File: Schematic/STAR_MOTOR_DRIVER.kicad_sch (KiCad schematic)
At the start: 50 parts, among them J1 6120XX21621_61200621621, J10 Optical Encoder 1, J11 Optical Encoder 2, J2 6120XX21621_61200621621, J3 1017491, J4 6120XX21621_61200821621, J5 6120XX21621_61200821621, J6 6120XX21621_61200821621, J7 1017491, J8 1017491, J9 1017491, U1 DRV8243SQDGQRQ1 (S-Variant), U2 DRV8243SQDGQRQ1 (S-Variant), U3 DRV8243SQDGQRQ1 (S-Variant), U4 DRV8243SQDGQRQ1 (S-Variant), U5 74LVC125APW_118

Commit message: Motor Driver PCB Design 1.0.0
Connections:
- net GND: now also J3.3 (2.1), J7.3 (2.1); no longer J3.2 (1.2), J7.2 (1.2)
- net MOTOR3_TERMINAL1: now also J9.1 (1.1); no longer J9.4 (2.2)
- net MOTOR3_TERMINAL2: now also J9.4 (2.2); no longer J9.1 (1.1)
- net MOTOR4_TERMINAL1: now also J8.1 (1.1); no longer J8.4 (2.2)
- net MOTOR4_TERMINAL2: now also J8.4 (2.2); no longer J8.1 (1.1)
- net P5V0_BUCK: now also J3.2 (1.2); no longer J3.3 (2.1)
- net P6V0_BUCK: now also J7.2 (1.2); no longer J7.3 (2.1)
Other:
- company: (none) -> Locked Inc.
- title: (none) -> Motor Driver

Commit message: Version 1.1.1
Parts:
- removed C13, C15, C17: 1u, Capacitor_SMD:C_0603_1608Metric_Pad1.08x0.95mm_HandSolder, symbol Device:C
- removed C14, C16, C18: 100n, Capacitor_SMD:C_0603_1608Metric_Pad1.08x0.95mm_HandSolder, symbol Device:C
- removed J1: 6120XX21621_61200621621, 61200621621:61200621621, symbol 61200621621:6120XX21621_61200621621
- removed J10: Optical Encoder 1, Connector_PinHeader_2.54mm:PinHeader_1x06_P2.54mm_Vertical, symbol Connector_Generic:Conn_01x06
- removed J11: Optical Encoder 2, Connector_PinHeader_2.54mm:PinHeader_1x06_P2.54mm_Vertical, symbol Connector_Generic:Conn_01x06
- removed J3, J8, J9: 1017491, 1017491, symbol 1017491:1017491
- removed U5: 74LVC125APW_118, 74LVC125APW,118:SOP65P640X110-14N, symbol 74LVC125APW-118:74LVC125APW_118
- added J1: 6120XX21621_61200821621, 6120XX21621_61200821621:61200821621, symbol 61200821621:6120XX21621_61200821621
- added J10, J3: B6B-XH-A, B6B_XH_A-2:JST_B6B-XH-A, symbol B6B-XH-A:B6B-XH-A
- added J11, J12: B6B-XH-A, B6B-XH-A:JST_B6B-XH-A, symbol B6B-XH-A:B6B-XH-A
- R10, R11, R12, R9: value 1k69 -> 3k16
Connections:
- net GND: now also J2.2, J2.4, J1.8, J10.2, J11.2, J12.2, J3.2; no longer J2.5
- net P3V3_BUCK: now also J2.1, J2.3, J2.5, J10.5, J11.5, J12.5, J3.5
- net ENCODER1_OUTPUT1 renamed MCU_ENCODER1_INPUT_B
- net MCU_ENCODER1_INPUT_B: now also J3.4
- net ENCODER1_OUTPUT2 renamed MCU_ENCODER2_INPUT_B
- net MCU_ENCODER2_INPUT_B: now also J10.4
- net ENCODER2_OUTPUT1 renamed MCU_ENCODER3_INPUT_B
- net MCU_ENCODER3_INPUT_B: now also J11.4
- net ENCODER2_OUTPUT2 renamed MCU_ENCODER4_INPUT_B
- net MCU_ENCODER4_INPUT_B: now also J12.4
- net MOTOR1_EN_IN1 renamed MCU_MOTOR1_EN_IN1
- net MOTOR1_IPROPI renamed MCU_MOTOR1_IPROPI
- net MOTOR1_PH_IN2 renamed MCU_MOTOR1_PH_IN2
- net MOTOR1_TERMINAL1 renamed MOTOR1_VCC
- net MOTOR1_VCC: now also J3.6; no longer J6.1
- net MOTOR1_TERMINAL2 renamed MOTOR1_VEE
- net MOTOR1_VEE: now also J3.1; no longer J6.3
- net MOTOR1_nCS renamed MCU_MOTOR1_nCS
- net MCU_MOTOR1_nCS: now also J1.1; no longer J2.1
- net MOTOR1_nFAULT renamed MCU_MOTOR1_nFAULT
- net MOTOR2_EN_IN1 renamed MCU_MOTOR2_EN_IN1
- net MOTOR2_IPROPI renamed MCU_MOTOR2_IPROPI
- net MOTOR2_PH_IN2 renamed MCU_MOTOR2_PH_IN2
- net MOTOR2_TERMINAL1 renamed MOTOR2_VCC
- net MOTOR2_VCC: now also J10.6; no longer J6.5
- net MOTOR2_TERMINAL2 renamed MOTOR2_VEE
- net MOTOR2_VEE: now also J10.1; no longer J6.7
- net MOTOR2_nCS renamed MCU_MOTOR2_nCS
- net MCU_MOTOR2_nCS: now also J1.3; no longer J2.2
- net MOTOR2_nFAULT renamed MCU_MOTOR2_nFAULT
- net MOTOR3_EN_IN1 renamed MCU_MOTOR3_EN_IN1
- net MOTOR3_IPROPI renamed MCU_MOTOR3_IPROPI
- net MOTOR3_PH_IN2 renamed MCU_MOTOR3_PH_IN2
- net MOTOR3_TERMINAL1 renamed MOTOR3_VCC
- net MOTOR3_VCC: now also J11.6
- net MOTOR3_TERMINAL2 renamed MOTOR3_VEE
- net MOTOR3_VEE: now also J11.1
- net MOTOR3_nCS renamed MCU_MOTOR3_nCS
- net MCU_MOTOR3_nCS: now also J1.5; no longer J2.4
- net MOTOR3_nFAULT renamed MCU_MOTOR3_nFAULT
- net MOTOR4_EN_IN1 renamed MCU_MOTOR4_EN_IN1
- net MOTOR4_IPROPI renamed MCU_MOTOR4_IPROPI
- net MOTOR4_PH_IN2 renamed MCU_MOTOR4_PH_IN2
- net MOTOR4_TERMINAL1 renamed MOTOR4_VCC
- net MOTOR4_VCC: now also J12.6
- net MOTOR4_TERMINAL2 renamed MOTOR4_VEE
- net MOTOR4_VEE: now also J12.1
- net MOTOR4_nCS renamed MCU_MOTOR4_nCS
- net MCU_MOTOR4_nCS: now also J1.7; no longer J2.3
- net MOTOR4_nFAULT renamed MCU_MOTOR4_nFAULT
- net SPI_CIPO renamed MCU_SPI_CIPO
- net MCU_SPI_CIPO: now also J1.6
- net SPI_COPI renamed MCU_SPI_COPI
- net MCU_SPI_COPI: now also J1.2
- net SPI_SCLK renamed MCU_SPI_SCLK
- net MCU_SPI_SCLK: now also J1.4
- new net MCU_ENCODER1_INPUT_A: J3.3, J6.1
- new net MCU_ENCODER2_INPUT_A: J10.3, J6.3
- new net MCU_ENCODER3_INPUT_A: J11.3, J6.5
- new net MCU_ENCODER4_INPUT_A: J12.3, J6.7
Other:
- note added: "input line is 20A, 4 motots, 3A eash, ADC overhead, 3.2A I_MCU_MOTOR = I_IPROPI x A_IPROPI 3.2A = I_IPROPI x 3075. I_PROPI=0.00104065 3.3V = 0.001041A x R, R = 3171.1 -> 3k16"
- note removed: "Input has to be 5V, output has to be 3V3"
- note removed: "input line is 20A, 4 motors, 5A each, ADC overhead, 6A I_motor = I_IPROPI x A_IPROPI 6A = I_IPROPI x 3075, I_IPROPI=0.00195121951 3.3V = 0.00195A x R, R = 1692.3 -> 1k69 WITH CODE: Shut off the motors at 4A"
- moved on the sheet: J2, J5, J6, J7

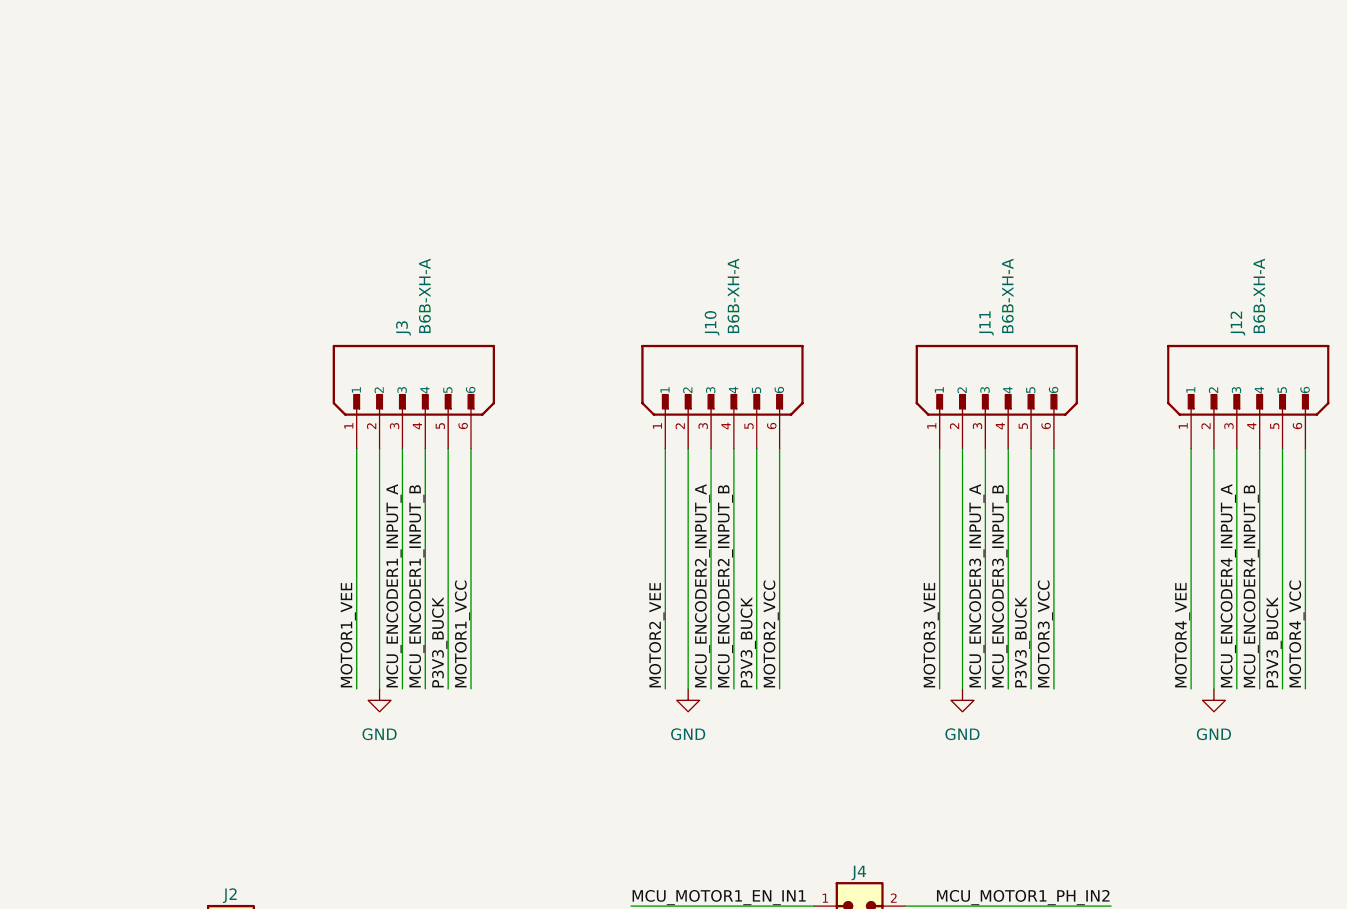
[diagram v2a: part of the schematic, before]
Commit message: V1.1.1 (Actual)
only changes are colors on schematic
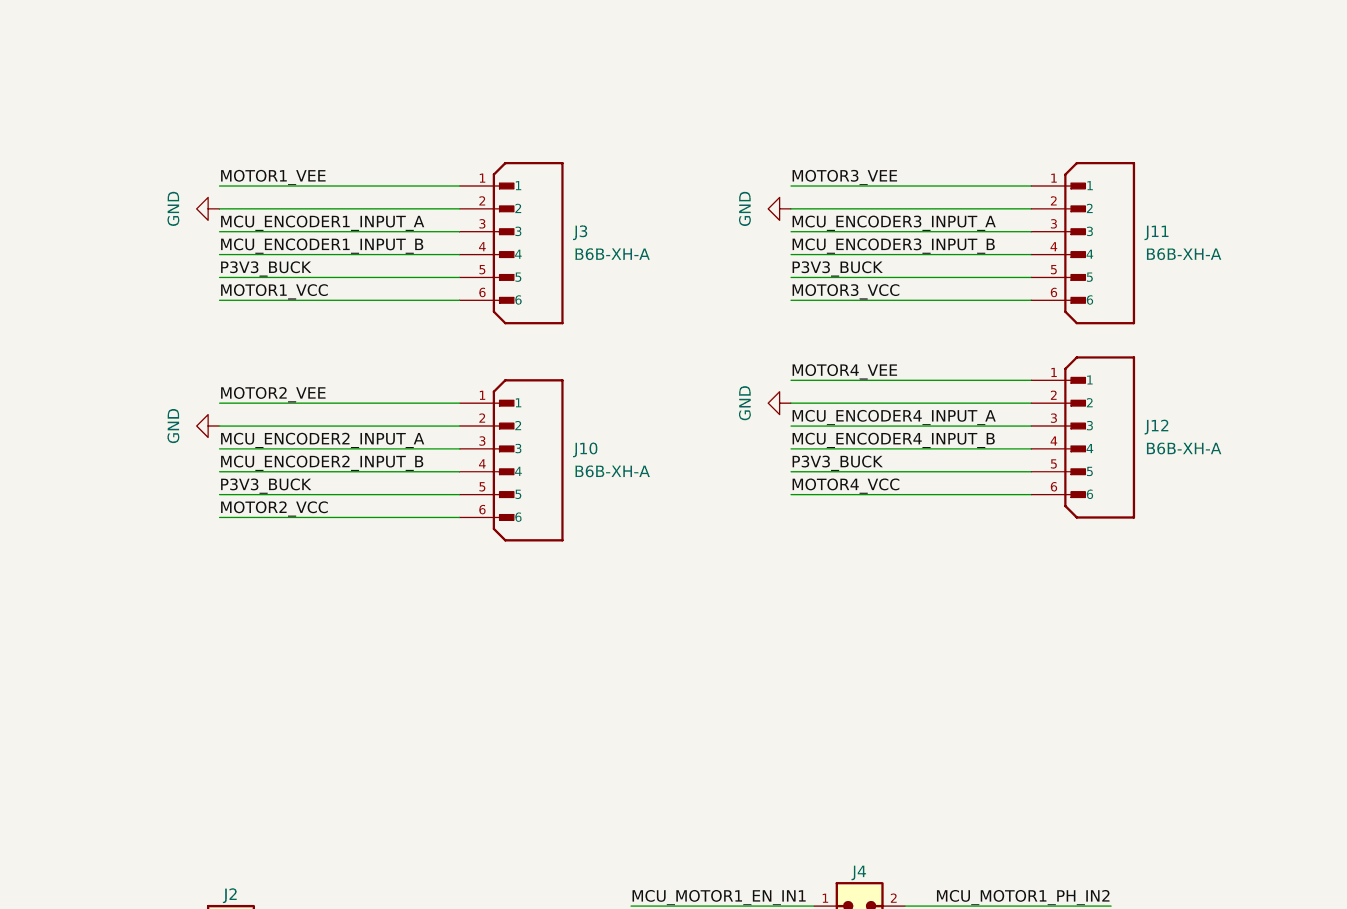
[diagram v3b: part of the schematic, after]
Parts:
- J1: footprint 6120XX21621_61200821621:61200821621 -> 61200821621:61200821621
- J11, J12: footprint B6B-XH-A:JST_B6B-XH-A -> B6B_XH_A-2:JST_B6B-XH-A
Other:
- moved on the sheet: J10, J11, J12, J3

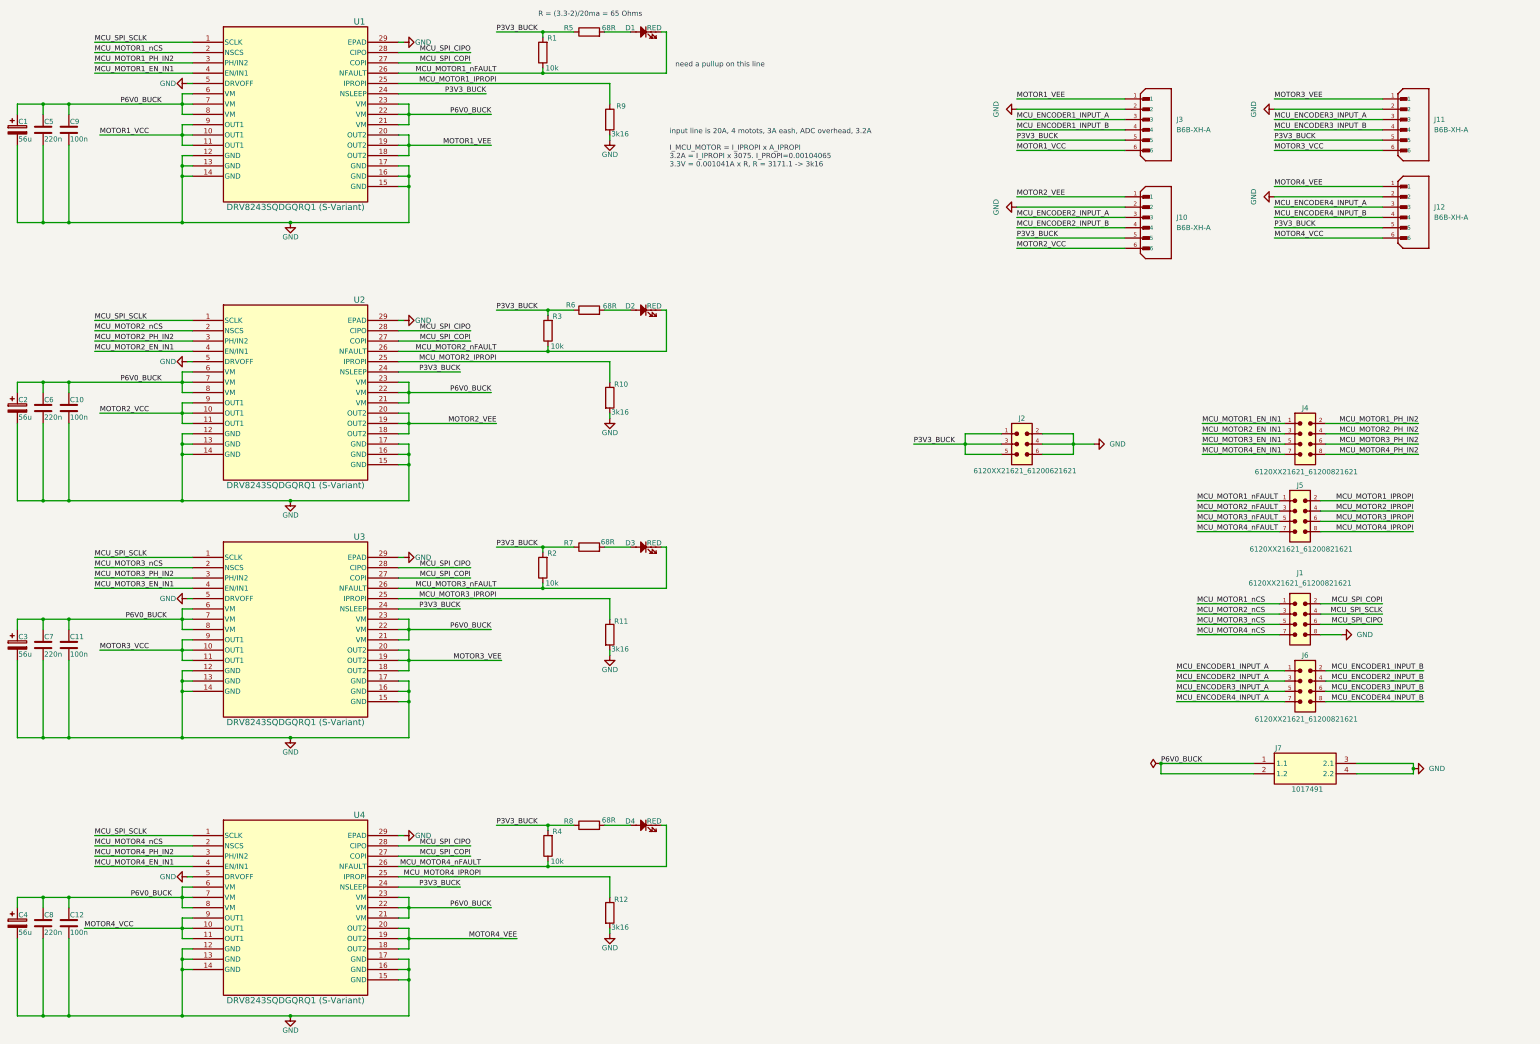
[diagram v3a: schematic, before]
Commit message: V1.1.1 (JUST ADDED BOXES AND TEXT AROUND CONNECTORS)
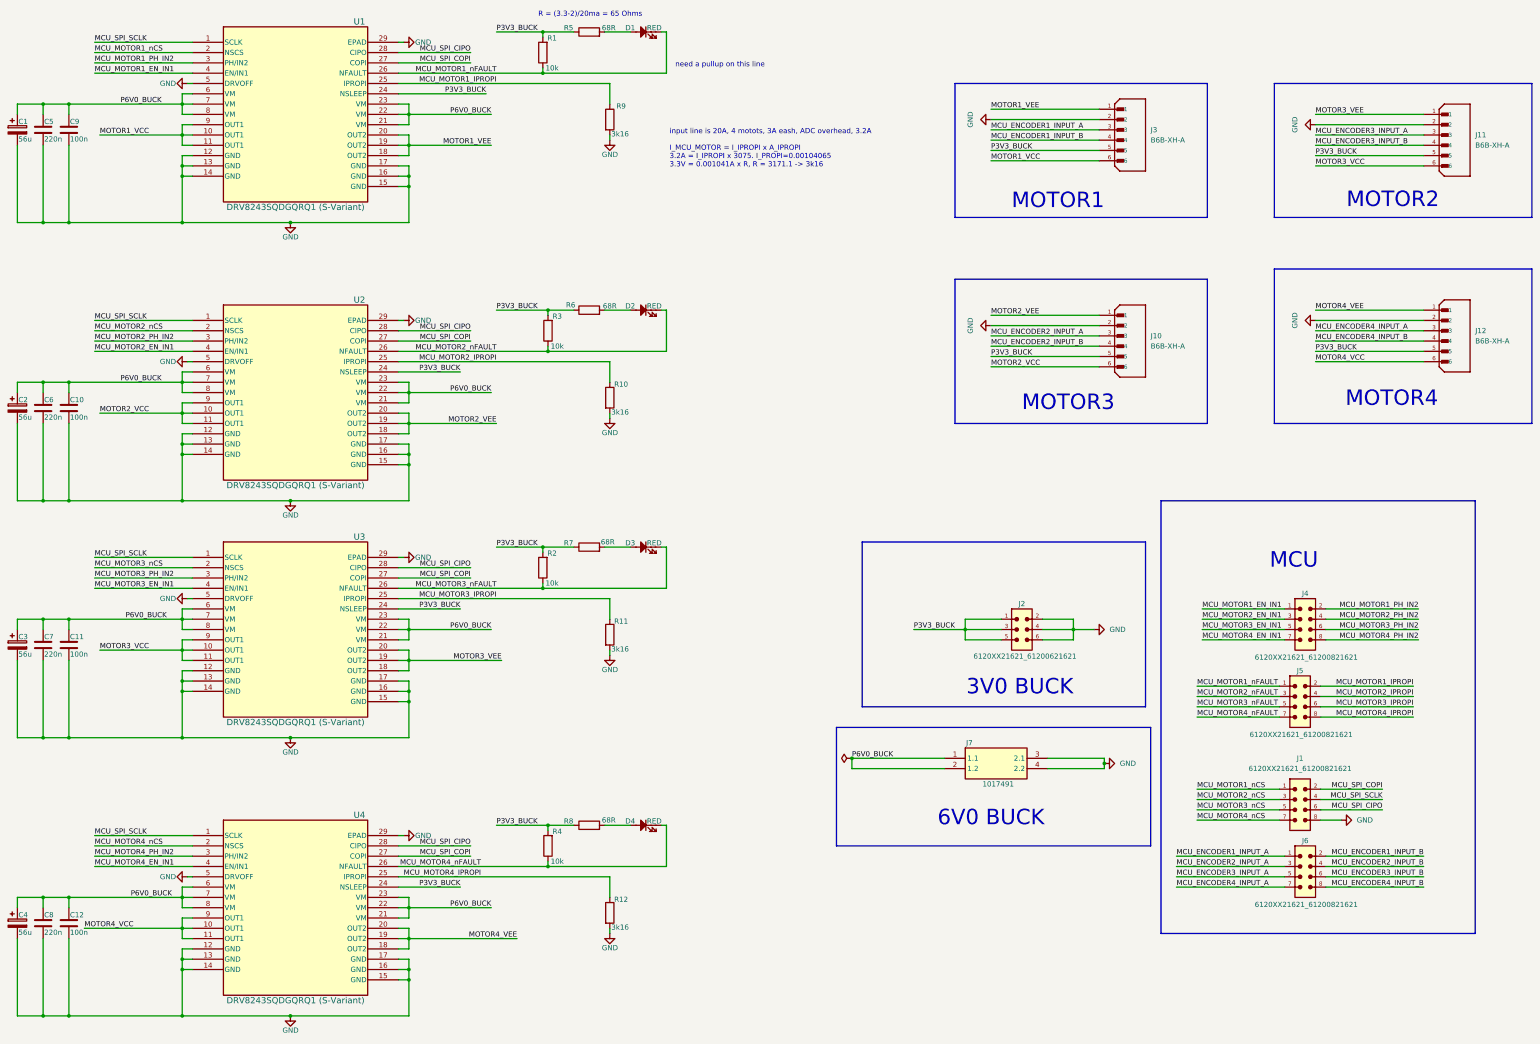
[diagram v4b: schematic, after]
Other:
- note added: "3V0 BUCK"
- note added: "6V0 BUCK"
- note added: "MCU"
- note added: "MOTOR1"
- note added: "MOTOR2"
- note added: "MOTOR3"
- note added: "MOTOR4"
- moved on the sheet: J1, J10, J11, J12, J2, J3, J4, J5, J6, J7
